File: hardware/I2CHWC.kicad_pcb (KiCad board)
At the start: 2 copper layers, 101 x 91.4 mm, 136 parts, among them J1 CONN_02X05, J10 CONN_02X20, J11 CONN_02X20, J12 CONN_02X20, J2 CONN_02X05, J3 CONN_02X05, J4 CONN_02X05, J5 CONN_02X05, J6 CONN_02X05, J7 CONN_02X05, J8 CONN_02X05, J9 CONN_02X03, SW1 I2C ADDR, U1 4051, U2 4051, U3 4051, U4 4051, U5 4051, U6 4051, U7 4051, U8 4051, U9 MapleMini

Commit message: Updates circuit schematic and PCB - wip.
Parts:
- removed D11, D12, D13, D14, D15, D16, D17, D18, D19, D20, D204, D61, D62, D63, D64, D65, D66, D67, D68, D69, D70, D71, D72, D73, D74, D75, D76, D77, D78, D79, D80, D81, D82, D83, D84, D85, D86, D87, D88, D89, D90, D91, D92, D93, D94, D95, D96, D97, D98: 1N4148, Diodes_SMD:D_MiniMELF_Handsoldering
- removed the D200 at (150.5, 51.2)
- removed J10, J11, J12: CONN_02X20, Pin_Headers:Pin_Header_Straight_2x20_Pitch2.54mm
- removed J7, J8: CONN_02X05, Pin_Headers:Pin_Header_Straight_2x05_Pitch2.54mm
- removed J9: CONN_02X03, Pin_Headers:Pin_Header_Straight_2x03_Pitch2.54mm
- removed U1, U2, U3, U4, U5, U6, U7, U8: 4051, Housings_SSOP:SOP-16_4.4x10.4mm_Pitch1.27mm
- added D200: 1N4148, Diode_THT:D_DO-35_SOD27_P10.16mm_Horizontal, F.Cu at (99.1, 86.4)
- added D200: 1N4148, Diode_THT:D_DO-35_SOD27_P10.16mm_Horizontal, F.Cu at (88.9, 86.4)
- added REF**: MountingHole_4.3mm_M4, MountingHole:MountingHole_4.3mm_M4, F.Cu at (106.7, 106.7)
- added REF**: MountingHole_4.3mm_M4, MountingHole:MountingHole_4.3mm_M4, F.Cu at (106.7, 17.8)
- added REF**: MountingHole_4.3mm_M4, MountingHole:MountingHole_4.3mm_M4, F.Cu at (17.8, 17.8)
- added REF**: MountingHole_4.3mm_M4, MountingHole:MountingHole_4.3mm_M4, F.Cu at (17.8, 106.7)
- D1, D10, D2, D201, D202, D203, D205, D206, D207, D21, D22, D23, D24, D25, D26, D27, D28, D29, D3, D30, D31, D32, D33, D34, D35, D36, D37, D38, D39, D4, D40, D41, D42, D43, D44, D45, D46, D47, D48, D49, D5, D50, D51, D52, D53, D54, D55, D56, D57, D58, D59, D6, D60, D7, D8, D9: footprint Diodes_SMD:D_MiniMELF_Handsoldering -> Diode_THT:D_DO-35_SOD27_P10.16mm_Horizontal
- J1: value CONN_02X05 -> I2C; footprint Pin_Headers:Pin_Header_Straight_2x05_Pitch2.54mm -> Connector_PinHeader_2.54mm:PinHeader_2x03_P2.54mm_Vertical
- J2: value CONN_02X05 -> INT SEL; footprint Pin_Headers:Pin_Header_Straight_2x05_Pitch2.54mm -> Connector_PinHeader_2.54mm:PinHeader_1x03_P2.54mm_Vertical
- J3: value CONN_02X05 -> ADC; footprint Pin_Headers:Pin_Header_Straight_2x05_Pitch2.54mm -> Connector_PinHeader_2.54mm:PinHeader_2x05_P2.54mm_Vertical
- J4: value CONN_02X05 -> EXT; footprint Pin_Headers:Pin_Header_Straight_2x05_Pitch2.54mm -> Connector_PinHeader_2.54mm:PinHeader_2x10_P2.54mm_Vertical
- J5: value CONN_02X05 -> Encoders 1-10; footprint Pin_Headers:Pin_Header_Straight_2x05_Pitch2.54mm -> Connector_PinHeader_2.54mm:PinHeader_2x20_P2.54mm_Vertical
- J6: value CONN_02X05 -> Switches 41-50; footprint Pin_Headers:Pin_Header_Straight_2x05_Pitch2.54mm -> Connector_PinHeader_2.54mm:PinHeader_2x20_P2.54mm_Vertical
- R1, R2, R3, R4, R5, R6, R7, R8: footprint Resistors_THT:R_Axial_DIN0204_L3.6mm_D1.6mm_P5.08mm_Horizontal -> Resistor_THT:R_Axial_DIN0204_L3.6mm_D1.6mm_P7.62mm_Horizontal
- SW1: value I2C ADDR -> CONFIG; footprint Buttons_Switches_SMD:SW_DIP_x8_W8.61mm_Slide_LowProfile -> Button_Switch_THT:SW_DIP_SPSTx08_Slide_9.78x22.5mm_W7.62mm_P2.54mm
- U9: footprint Housings_DIP:DIP-40_W15.24mm -> Package_DIP:DIP-40_W15.24mm
- moved J2 83.8 mm to (99.1, 15.2)
- moved J1 75.0 mm to (91.4, 17.8), turned to 270 degrees
- moved D201 62.2 mm to (96.5, 86.4), turned to 270 degrees
- moved D202 62.2 mm to (94.0, 86.4)
- moved SW1 58.0 mm to (99.1, 101.6), turned to 270 degrees
- moved J4 47.7 mm to (45.7, 20.3), turned to 90 degrees
- moved U9 47.0 mm to (83.8, 27.9)
- moved R8 45.5 mm to (27.9, 25.8), turned to 270 degrees
- moved D10 44.5 mm to (63.5, 66.0)
- moved D4 44.5 mm to (33.0, 66.0)
- moved D5 44.5 mm to (38.1, 66.0)
- moved D6 44.5 mm to (43.2, 66.0)
- moved D7 44.5 mm to (48.3, 66.0)
- moved D8 44.5 mm to (53.3, 66.0)
- moved D1 44.4 mm to (17.8, 66.0)
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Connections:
- D1 pad 1: MatrixIn2 -> EncIn1b
- D10 pad 1: MatrixIn2 -> EncIn1b
- D2 pad 1: MatrixIn2 -> EncIn1b
- D201 pad 1: MatrixIn2 -> ConfigIn
- D202 pad 1: MatrixIn3 -> ConfigIn
- D203 pad 1: MatrixIn4 -> ConfigIn
- D205 pad 1: MatrixIn6 -> ConfigIn
- D206 pad 1: MatrixIn7 -> ConfigIn
- D207 pad 1: MatrixIn8 -> ConfigIn
- D21 pad 1: MatrixIn1 -> SwitchIn1
- D22 pad 1: MatrixIn3 -> EncIn1a
- D23 pad 1: MatrixIn1 -> SwitchIn1
- D24 pad 1: MatrixIn3 -> EncIn1a
- D25 pad 1: MatrixIn1 -> SwitchIn1
- D26 pad 1: MatrixIn3 -> EncIn1a
- D27 pad 1: MatrixIn1 -> SwitchIn1
- D28 pad 1: MatrixIn3 -> EncIn1a
- D29 pad 1: MatrixIn1 -> SwitchIn1
- D3 pad 1: MatrixIn2 -> EncIn1b
- D30 pad 1: MatrixIn3 -> EncIn1a
- D31 pad 1: MatrixIn1 -> SwitchIn1
- D32 pad 1: MatrixIn3 -> EncIn1a
- D33 pad 1: MatrixIn1 -> SwitchIn1
- D34 pad 1: MatrixIn3 -> EncIn1a
- D35 pad 1: MatrixIn1 -> SwitchIn1
- D36 pad 1: MatrixIn3 -> EncIn1a
- D37 pad 1: MatrixIn1 -> SwitchIn1
- D38 pad 1: MatrixIn3 -> EncIn1a
- D39 pad 1: MatrixIn1 -> SwitchIn1
- D4 pad 1: MatrixIn2 -> EncIn1b
- D40 pad 1: MatrixIn3 -> EncIn1a
- D41 pad 1: MatrixIn4 -> SwitchIn4
- D42 pad 1: MatrixIn6 -> SwitchIn4
- D43 pad 1: MatrixIn4 -> SwitchIn4
- D44 pad 1: MatrixIn6 -> SwitchIn4
- D45 pad 1: MatrixIn4 -> SwitchIn4
- D46 pad 1: MatrixIn6 -> SwitchIn4
- D47 pad 1: MatrixIn4 -> SwitchIn4
- D48 pad 1: MatrixIn6 -> SwitchIn4
- D49 pad 1: MatrixIn4 -> SwitchIn4
- D5 pad 1: MatrixIn2 -> EncIn1b
- D50 pad 1: MatrixIn6 -> SwitchIn4
- D51 pad 1: MatrixIn4 -> SwitchIn5
- D52 pad 1: MatrixIn6 -> SwitchIn5
- D53 pad 1: MatrixIn4 -> SwitchIn5
- D54 pad 1: MatrixIn6 -> SwitchIn5
- D55 pad 1: MatrixIn4 -> SwitchIn5
- D56 pad 1: MatrixIn6 -> SwitchIn5
- D57 pad 1: MatrixIn4 -> SwitchIn5
- D58 pad 1: MatrixIn6 -> SwitchIn5
- D59 pad 1: MatrixIn4 -> SwitchIn5
- D6 pad 1: MatrixIn2 -> EncIn1b
- D60 pad 1: MatrixIn6 -> SwitchIn5
- D7 pad 1: MatrixIn2 -> EncIn1b
- D8 pad 1: MatrixIn2 -> EncIn1b
- D9 pad 1: MatrixIn2 -> EncIn1b
- J1 pad 5: Net-(J1-Pad5) -> GND
- J2 pad 1: Net-(J2-Pad1) -> Net-(J1-Pad2)
- J2 pad 3: Net-(J2-Pad3) -> Net-(J1-Pad4)
- J3 pad 1: Net-(J3-Pad1) -> ADC1
- J3 pad 10: GNDA -> +3.3VA
- J3 pad 2: Net-(J3-Pad2) -> ADC2
- J3 pad 3: Net-(J3-Pad3) -> ADC3
- J3 pad 4: Net-(J3-Pad4) -> ADC4
- J3 pad 5: Net-(J3-Pad5) -> ADC5
- J3 pad 6: Net-(J3-Pad6) -> ADC6
- J3 pad 7: Net-(J3-Pad7) -> ADC7
- J3 pad 8: Net-(J3-Pad8) -> ADC8
- J3 pad 9: +3.3VA -> GNDA
- J4 pad 1: Net-(J4-Pad1) -> MatrixOut1
- J4 pad 10: GNDA -> MatrixOut10
- J4 pad 2: Net-(J4-Pad2) -> MatrixOut2
- J4 pad 3: Net-(J4-Pad3) -> MatrixOut3
- J4 pad 4: Net-(J4-Pad4) -> MatrixOut4
- J4 pad 5: Net-(J4-Pad5) -> MatrixOut5
- J4 pad 6: Net-(J4-Pad6) -> MatrixOut6
- J4 pad 7: Net-(J4-Pad7) -> MatrixOut7
- J4 pad 8: Net-(J4-Pad8) -> MatrixOut8
- J4 pad 9: +3.3VA -> MatrixOut9
- J5 pad 1: Net-(J5-Pad1) -> Net-(D21-Pad2)
- J5 pad 10: GNDA -> Net-(D3-Pad2)
- J5 pad 2: Net-(J5-Pad2) -> Net-(D1-Pad2)
- J5 pad 3: Net-(J5-Pad3) -> Net-(D22-Pad2)
- J5 pad 4: Net-(J5-Pad4) -> MatrixOut1
- J5 pad 5: Net-(J5-Pad5) -> Net-(D23-Pad2)
- J5 pad 6: Net-(J5-Pad6) -> Net-(D2-Pad2)
- J5 pad 7: Net-(J5-Pad7) -> Net-(D24-Pad2)
- J5 pad 8: Net-(J5-Pad8) -> MatrixOut2
- J5 pad 9: +3.3VA -> Net-(D25-Pad2)
- J6 pad 1: Net-(J6-Pad1) -> Net-(D41-Pad2)
- J6 pad 10: GNDA -> MatrixOut5
- J6 pad 2: Net-(J6-Pad2) -> MatrixOut1
- J6 pad 3: Net-(J6-Pad3) -> Net-(D42-Pad2)
- J6 pad 4: Net-(J6-Pad4) -> MatrixOut2
- J6 pad 5: Net-(J6-Pad5) -> Net-(D43-Pad2)
- J6 pad 6: Net-(J6-Pad6) -> MatrixOut3
- J6 pad 7: Net-(J6-Pad7) -> Net-(D44-Pad2)
- J6 pad 8: Net-(J6-Pad8) -> MatrixOut4
- J6 pad 9: +3.3VA -> Net-(D45-Pad2)
- R1 pad 1: ADC0 -> ADC1
- R2 pad 1: ADC1 -> ADC8
- R3 pad 1: ADC2 -> ADC3
- R4 pad 1: ADC3 -> ADC6
- R5 pad 1: ADC4 -> ADC5
- R6 pad 1: ADC5 -> ADC4
- R7 pad 1: ADC6 -> ADC7
- R8 pad 1: ADC7 -> ADC2
- SW1 pad 1: MatrixOut11 -> Net-(D200-Pad2)
- SW1 pad 10: Net-(D201-Pad2) -> MatrixOut7
- SW1 pad 11: Net-(D202-Pad2) -> MatrixOut6
- SW1 pad 12: Net-(D203-Pad2) -> MatrixOut5
- SW1 pad 13: Net-(D204-Pad2) -> MatrixOut4
- SW1 pad 14: Net-(D205-Pad2) -> MatrixOut3
- SW1 pad 15: Net-(D206-Pad2) -> MatrixOut2
- SW1 pad 16: Net-(D207-Pad2) -> MatrixOut1
- SW1 pad 2: MatrixOut11 -> Net-(D201-Pad2)
- SW1 pad 3: MatrixOut11 -> Net-(D202-Pad2)
- SW1 pad 4: MatrixOut11 -> Net-(D203-Pad2)
- SW1 pad 5: MatrixOut11 -> Net-(D204-Pad2)
- SW1 pad 6: MatrixOut11 -> Net-(D205-Pad2)
- SW1 pad 7: MatrixOut11 -> Net-(D206-Pad2)
- SW1 pad 8: MatrixOut11 -> Net-(D207-Pad2)
- SW1 pad 9: Net-(D200-Pad2) -> MatrixOut8
- U9 pad 10: ADC2 -> ADC3
- U9 pad 11: ADC3 -> ADC4
- U9 pad 12: ADC4 -> ADC5
- U9 pad 13: ADC5 -> ADC6
- U9 pad 14: ADC6 -> ADC7
- U9 pad 15: ADC7 -> ADC8
- U9 pad 16: MatrixIn9 -> EncIn2b
- U9 pad 17: (no net) -> EncIn2a
- U9 pad 18: (no net) -> EncIn1b
- U9 pad 19: (no net) -> EncIn1a
- U9 pad 20: Net-(J9-Pad6) -> Net-(J1-Pad6)
- U9 pad 21: MatrixOut11 -> SwitchIn5
- U9 pad 22: MatrixOut10 -> SwitchIn4
- U9 pad 23: MatrixOut9 -> SwitchIn3
- U9 pad 24: MatrixOut8 -> SwitchIn2
- U9 pad 25: MatrixOut7 -> SwitchIn1
- U9 pad 26: MatrixOut6 -> MatrixOut10
- U9 pad 27: MatrixOut5 -> MatrixOut9
- U9 pad 28: MatrixOut4 -> MatrixOut8
- U9 pad 29: MatrixOut3 -> MatrixOut7
- U9 pad 30: MatrixOut2 -> MatrixOut6
- U9 pad 31: MatrixOut1 -> MatrixOut5
- U9 pad 32: MatrixIn4 -> MatrixOut4
- U9 pad 33: MatrixIn3 -> MatrixOut3
- U9 pad 34: MatrixIn2 -> MatrixOut2
- U9 pad 35: MatrixIn1 -> MatrixOut1
- U9 pad 36: Net-(J9-Pad5) -> Net-(J1-Pad3)
- U9 pad 37: Net-(J9-Pad3) -> Net-(J1-Pad1)
- U9 pad 38: Net-(J9-Pad1) -> Net-(J2-Pad2)
- U9 pad 4: MatrixIn6 -> ConfigIn
- U9 pad 5: MatrixIn7 -> EncIn3b
- U9 pad 6: MatrixIn8 -> EncIn3a
- U9 pad 8: ADC0 -> ADC1
- U9 pad 9: ADC1 -> ADC2
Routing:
- net MatrixIn1: track 109.2 -> 0.00 mm
- net MatrixIn2: track 79.2 -> 0.00 mm
- net MatrixIn3: track 76.3 -> 0.00 mm
- net ADC0: track 52.5 -> 0.00 mm
- net ADC6: track 50.5 -> 0.00 mm, vias 3 -> 0
- net ADC1: track 38.7 -> 0.00 mm
- net ADC5: track 38.4 -> 0.00 mm
- net GNDA: track 46.6 -> 17.8 mm
- net ADC4: track 26.4 -> 0.00 mm
- net ADC2: track 27.8 -> 1.51 mm
- net SwitchIn5: track 0.00 -> 22.9 mm
- net SwitchIn4: track 0.00 -> 22.9 mm
- net ConfigIn: track 0.00 -> 17.8 mm
- net Net-(J1-Pad7): track 16.3 -> 0.00 mm, vias 1 -> 0
- net Net-(J1-Pad5): track 15.8 -> 0.00 mm, vias 1 -> 0
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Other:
- board size 101 x 91.4 mm -> 99.1 x 99.1 mm
- board text added: "Extension"
- board text added: "I2C/Power"
- board text added: "Potentiometers"
- board text added: "riban © 2019 I2C HWC 0.1"

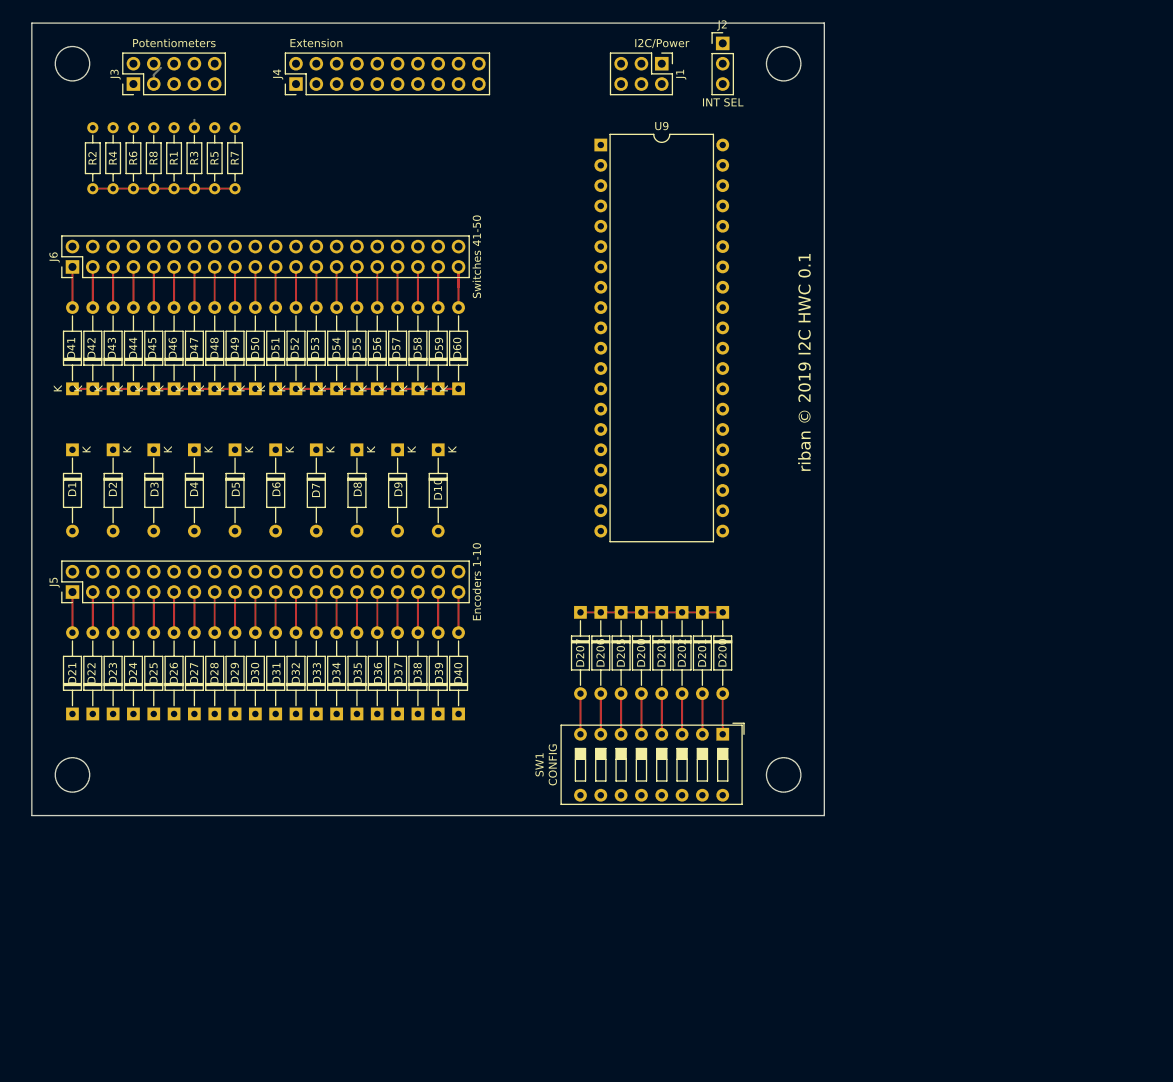
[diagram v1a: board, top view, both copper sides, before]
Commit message: Firmwware changes: Temporarily disable ADC (whilst investigating noise issues). Change quantity of switches (from 60 to 50). Start implementing I2C commands (wip). Reverse encoder rotation (maybe just the hardware implementation of the prototype - need to validate with schematics). Schematic and PCB improvements (wip): Separate out main and extender boards to separate projects / folders. Main board now supports 10 encoders with switches, 20 switches and 8 ADC plus detection of ADC multiplex and I2C address. Extension board for encoders 11 - 30. Extension board for ADC 1 - 64.
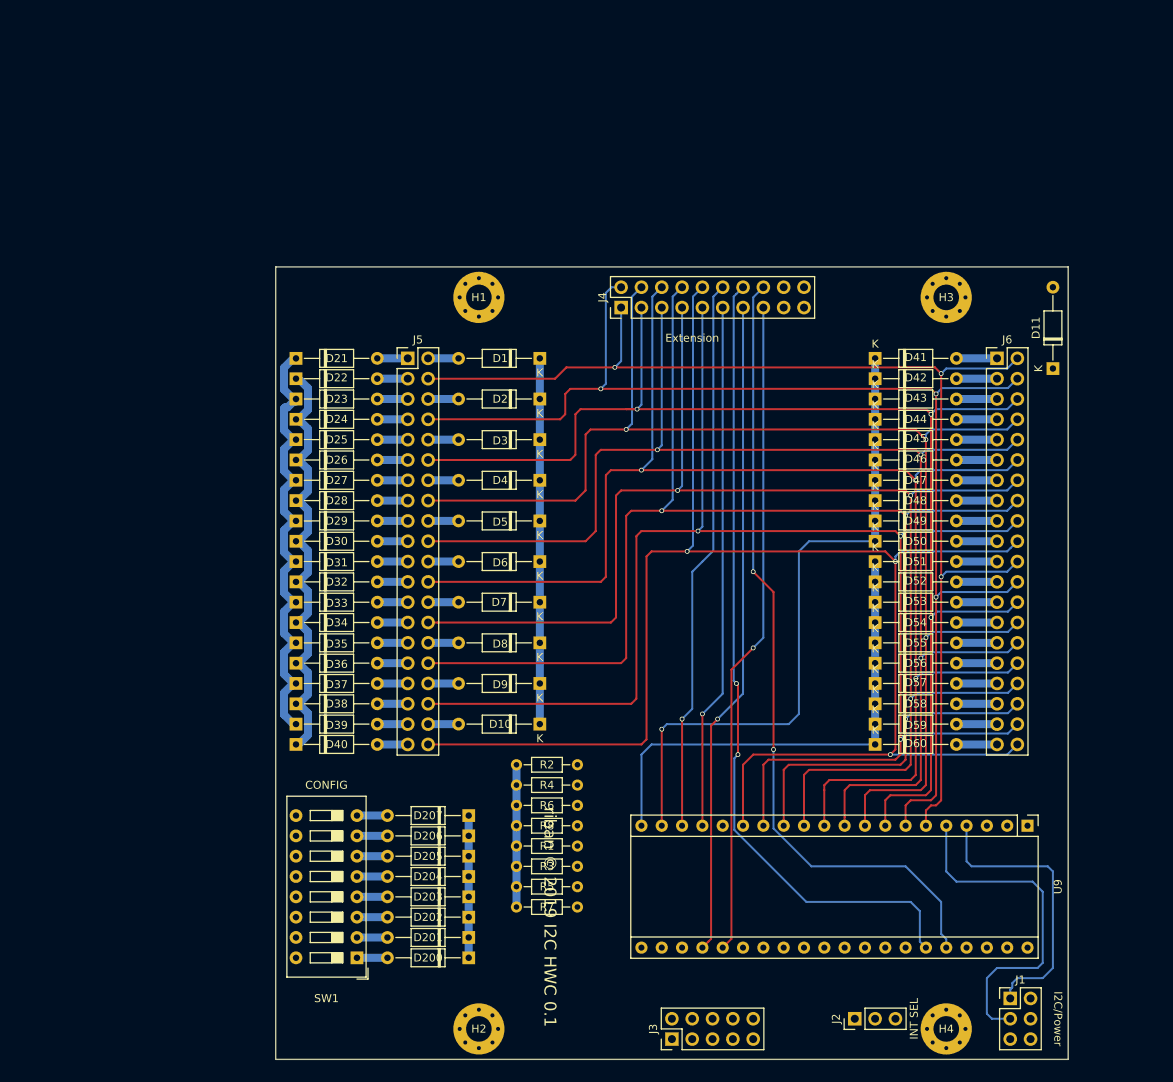
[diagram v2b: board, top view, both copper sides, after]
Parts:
- removed the D200 at (99.1, 86.4)
- removed the D200 at (88.9, 86.4)
- removed REF** (x4): MountingHole_4.3mm_M4, MountingHole:MountingHole_4.3mm_M4
- added D11: 1N4148, Diode_THT:D_DO-35_SOD27_P10.16mm_Horizontal, F.Cu at (140.3, 55.9)
- added D200: 1N4148, Diode_THT:D_DO-35_SOD27_P10.16mm_Horizontal, F.Cu at (67.3, 129.5)
- added D204: 1N4148, Diode_THT:D_DO-35_SOD27_P10.16mm_Horizontal, F.Cu at (67.3, 119.4)
- added H1: MountingHole_Pad, MountingHole:MountingHole_3.2mm_M3_Pad_Via, F.Cu at (68.6, 47.0)
- added H2: MountingHole_Pad, MountingHole:MountingHole_3.2mm_M3_Pad_Via, F.Cu at (68.6, 138.4)
- added H3: MountingHole_Pad, MountingHole:MountingHole_3.2mm_M3_Pad_Via, F.Cu at (127.0, 47.0)
- added H4: MountingHole_Pad, MountingHole:MountingHole_3.2mm_M3_Pad_Via, F.Cu at (127.0, 138.4)
- J1: value I2C -> PWR/I2C
- U9: value MapleMini -> Maple_Mini; footprint Package_DIP:DIP-40_W15.24mm -> Module:Maple_Mini
- moved J3 137.0 mm to (92.7, 139.7)
- moved J1 124.7 mm to (135.0, 134.6), turned to 0 degrees
- moved J2 123.0 mm to (115.6, 137.2), turned to 90 degrees
- moved J6 116.1 mm to (133.3, 54.6), turned to 0 degrees
- moved R7 106.4 mm to (80.9, 123.2), turned to 180 degrees
- moved R5 105.1 mm to (80.9, 120.7), turned to 180 degrees
- moved R3 104.0 mm to (80.9, 118.1), turned to 180 degrees
- moved R1 103.0 mm to (80.9, 115.6), turned to 180 degrees
- moved R8 102.1 mm to (80.9, 113.0), turned to 180 degrees
- moved R6 101.3 mm to (80.9, 110.5), turned to 180 degrees
- moved R4 100.6 mm to (80.9, 108.0), turned to 180 degrees
- moved U9 100.4 mm to (137.2, 113.0), turned to 270 degrees
- moved D41 100.4 mm to (118.1, 54.6), turned to 0 degrees
- moved R2 100.1 mm to (80.9, 105.4), turned to 180 degrees
- moved D42 97.8 mm to (118.1, 57.1), turned to 0 degrees
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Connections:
- J4 pad 18: ConfigIn -> Net-(D11-Pad2)
- U9 pad 1: +3.3VA -> +3V3
- U9 pad 10: ADC3 -> MatrixOut5
- U9 pad 11: ADC4 -> MatrixOut6
- U9 pad 12: ADC5 -> MatrixOut7
- U9 pad 13: ADC6 -> MatrixOut8
- U9 pad 14: ADC7 -> MatrixOut9
- U9 pad 15: ADC8 -> MatrixOut10
- U9 pad 16: EncIn2b -> SwitchIn1
- U9 pad 17: EncIn2a -> SwitchIn2
- U9 pad 18: EncIn1b -> SwitchIn3
- U9 pad 19: EncIn1a -> SwitchIn4
- U9 pad 2: GNDA -> GND
- U9 pad 20: Net-(J1-Pad6) -> SwitchIn5
- U9 pad 21: SwitchIn5 -> Net-(J1-Pad6)
- U9 pad 22: SwitchIn4 -> EncIn1a
- U9 pad 23: SwitchIn3 -> EncIn1b
- U9 pad 24: SwitchIn2 -> EncIn2a
- U9 pad 25: SwitchIn1 -> EncIn2b
- U9 pad 26: MatrixOut10 -> ADC8
- U9 pad 27: MatrixOut9 -> ADC7
- U9 pad 28: MatrixOut8 -> ADC6
- U9 pad 29: MatrixOut7 -> ADC5
- U9 pad 3: (no net) -> Net-(J2-Pad2)
- U9 pad 30: MatrixOut6 -> ADC4
- U9 pad 31: MatrixOut5 -> ADC3
- U9 pad 32: MatrixOut4 -> ADC2
- U9 pad 33: MatrixOut3 -> ADC1
- U9 pad 34: MatrixOut2 -> (no net)
- U9 pad 35: MatrixOut1 -> EncIn3a
- U9 pad 36: Net-(J1-Pad3) -> EncIn3b
- U9 pad 37: Net-(J1-Pad1) -> ConfigIn
- U9 pad 38: Net-(J2-Pad2) -> (no net)
- U9 pad 39: GND -> GNDA
- U9 pad 4: ConfigIn -> Net-(J1-Pad1)
- U9 pad 40: +3V3 -> +3.3VA
- U9 pad 5: EncIn3b -> Net-(J1-Pad3)
- U9 pad 6: EncIn3a -> MatrixOut1
- U9 pad 7: (no net) -> MatrixOut2
- U9 pad 8: ADC1 -> MatrixOut3
- U9 pad 9: ADC2 -> MatrixOut4
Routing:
- net MatrixOut10: track 0.00 -> 200.2 mm, vias 0 -> 3
- net MatrixOut9: track 0.00 -> 191.7 mm, vias 0 -> 3
- net MatrixOut8: track 0.00 -> 190.0 mm, vias 0 -> 3
- net MatrixOut7: track 0.00 -> 181.6 mm, vias 0 -> 3
- net MatrixOut6: track 0.00 -> 180.1 mm, vias 0 -> 3
- net MatrixOut5: track 0.00 -> 171.0 mm, vias 0 -> 3
- net MatrixOut4: track 0.00 -> 169.3 mm, vias 0 -> 3
- net MatrixOut3: track 0.00 -> 162.6 mm, vias 0 -> 3
- net MatrixOut2: track 0.00 -> 160.2 mm, vias 0 -> 3
- net MatrixOut1: track 0.00 -> 151.1 mm, vias 0 -> 3
- net EncIn3a: track 0.00 -> 101.0 mm, vias 0 -> 2
- net EncIn3b: track 0.00 -> 100.0 mm, vias 0 -> 2
- net EncIn2b: track 0.00 -> 82.1 mm, vias 0 -> 1
- net EncIn2a: track 0.00 -> 82.1 mm, vias 0 -> 1
- net SwitchIn3: track 0.00 -> 69.4 mm, vias 0 -> 1
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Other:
- board text removed: "Potentiometers"
